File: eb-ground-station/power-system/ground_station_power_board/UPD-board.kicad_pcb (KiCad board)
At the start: 2 copper layers, 140.7 x 86.5 mm, 185 parts, among them J1 Conn_01x04, J10 PI 1827486, J11 PC 1720806, J12 Conn_02x02_Odd_Even, J13 Conn_01x05, J14 Conn_01x04, J2 Conn_01x03, J3 Conn_01x03, J4 Conn_01x03, J5 Conn_01x03, J6 Conn_01x03, J7 PI 1924143, J8 PI 1827923, J9 PI 1827486, Q1 DMN61D8L-LVT, Q10 DMN61D8L-LVT, Q11 SUD50P08-25L-E3, Q12 SUD50P08-25L-E3, Q13 DMN61D8L-LVT, Q14 DMN61D8L-LVT, Q15 DMN61D8L-LVT, Q16 DMN61D8L-LVT, Q17 DMN61D8L-LVT, Q18 DMN61D8L-LVT, Q19 DMN61D8L-LVT, Q2 SUD50P08-25L-E3, Q20 DMN61D8L-LVT, Q21 SUD50P08-25L-E3, Q22 SUD50P08-25L-E3, Q3 SUD50P08-25L-E3, Q4 DMN61D8L-LVT, Q5 SUD50P08-25L-E3, Q6 SUD50P08-25L-E3, Q7 DMN61D8L-LVT, Q8 SUD50P08-25L-E3, Q9 SUD50P08-25L-E3, U1 MAX7310, U10 TC4427, U11 TC4427, U12 TC4427, U13 TC4427, U14 TC4427, U15 TC4427, U2 MAX7310, U3 MAX7310, U4 ADT7410TRZ, U5 ADS1115IDGS, U6 UA78M33, U7 U_RasPi_40pin, U8 TC4427, U9 TC4427

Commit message: Cleaned up the repo
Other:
- board text removed: "Different analog connector"
- board text removed: "TODO:"
- board text removed: "Too many vias in high current traces?"
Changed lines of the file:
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@@
-    (effects (font (size 1.5 1.5) (thickness 0.3)))
-  )
-  (gr_text "Different analog connector" (at 29.4386 21.4122) (layer "F.Cu")
-    (effects (font (size 1.5 1.5) (thickness 0.3)))
-  )
-  (gr_text "TODO:" (at 20.955 16.5608) (layer "F.Cu")
-    (effects (font (size 3 3) (thickness 0.3)))
-  )
-  (gr_text "Too many vias in high current traces?" (at 35.9156 24.9174) (layer "F.Cu")
     (effects (font (size 1.5 1.5) (thickness 0.3)))
   )

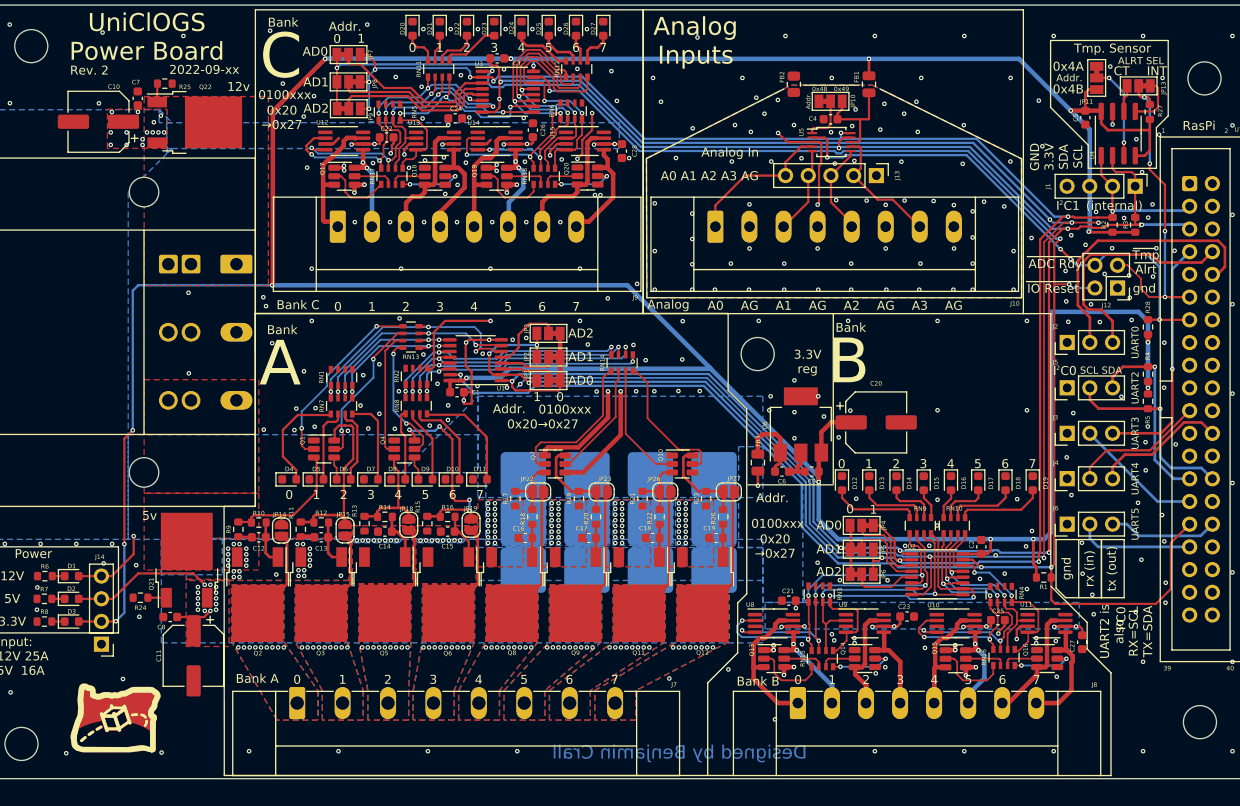
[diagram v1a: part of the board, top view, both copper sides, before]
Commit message: Fixed UPD board, ready for review and ordering
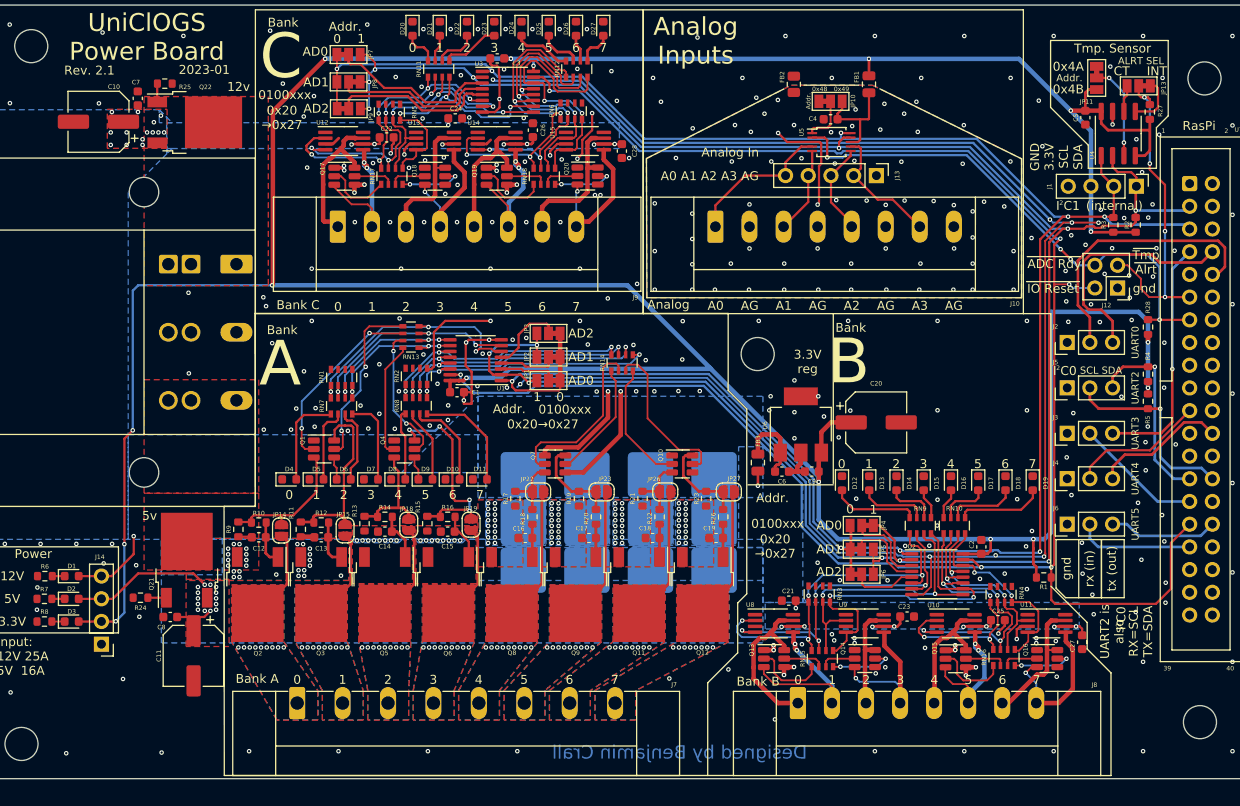
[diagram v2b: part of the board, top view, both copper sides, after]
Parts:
- removed LOGO1: OreSat Logo, oresat-footprints:logo-small
- moved R2 2.59 mm to (203.3, 77.8)
- moved R3 2.45 mm to (200.8, 77.8)
- moved J1 0.14 mm to (203.4, 73.5)
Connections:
- J1 pad 1: SCL -> SDA
- J1 pad 2: SDA -> SCL
- Q1 pad 2: MOS_A0 -> MOS_A1
- Q1 pad 5: MOS_A1 -> MOS_A0
- Q10 pad 2: MOS_A6 -> MOS_A7
- Q10 pad 5: MOS_A7 -> MOS_A6
- Q13 pad 3: OUT_B0 -> OUT_B1
- Q13 pad 6: OUT_B1 -> OUT_B0
- Q14 pad 3: OUT_B2 -> OUT_B3
- Q14 pad 6: OUT_B3 -> OUT_B2
- Q15 pad 3: OUT_B4 -> OUT_B5
- Q15 pad 6: OUT_B5 -> OUT_B4
- Q16 pad 3: OUT_B6 -> OUT_B7
- Q16 pad 6: OUT_B7 -> OUT_B6
- Q17 pad 3: OUT_C0 -> OUT_C1
- Q17 pad 6: OUT_C1 -> OUT_C0
- Q18 pad 3: OUT_C2 -> OUT_C3
- Q18 pad 6: OUT_C3 -> OUT_C2
- Q19 pad 3: OUT_C4 -> OUT_C5
- Q19 pad 6: OUT_C5 -> OUT_C4
- Q20 pad 3: OUT_C6 -> OUT_C7
- Q20 pad 6: OUT_C7 -> OUT_C6
- Q4 pad 2: MOS_A2 -> MOS_A3
- Q4 pad 5: MOS_A3 -> MOS_A2
- Q7 pad 2: MOS_A4 -> MOS_A5
- Q7 pad 5: MOS_A5 -> MOS_A4
- U4 pad 1: SDA -> SCL
- U4 pad 2: SCL -> SDA
- U5 pad 10: SDA -> SCL
- U5 pad 9: SCL -> SDA
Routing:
- net OUT_B1: track 12.4 -> 21.4 mm
- net OUT_B3: track 10.1 -> 17.2 mm, vias 0 -> 1
- net MOS_A5: track 13.1 -> 19.7 mm
- net OUT_C1: track 11.4 -> 16.5 mm
- net OUT_B5: track 11.4 -> 16.0 mm
- net MOS_A6: track 13.6 -> 18.2 mm
- net OUT_B7: track 12.4 -> 16.8 mm, vias 0 -> 1
- net OUT_C5: track 11.3 -> 15.6 mm
- net SCL: track 256.6 -> 252.3 mm
- net OUT_C3: track 10.9 -> 15.0 mm, vias 0 -> 1
- net MOS_A1: track 16.9 -> 21.0 mm
- net MOS_A4: track 17.2 -> 13.2 mm
- net OUT_C7: track 12.1 -> 15.8 mm, vias 0 -> 1
- net SDA: track 254.0 -> 256.7 mm, vias 14 -> 13
- net MOS_A7: track 16.0 -> 13.9 mm
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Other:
- board text added: "2023-01"
- board text added: "GND 3.3V SCL SDA"
- board text added: "Rev. 2.1"
- board text removed: "2022-09-xx"
- board text removed: "GND 3.3V SDA SCL"
- board text removed: "Rev. 2"

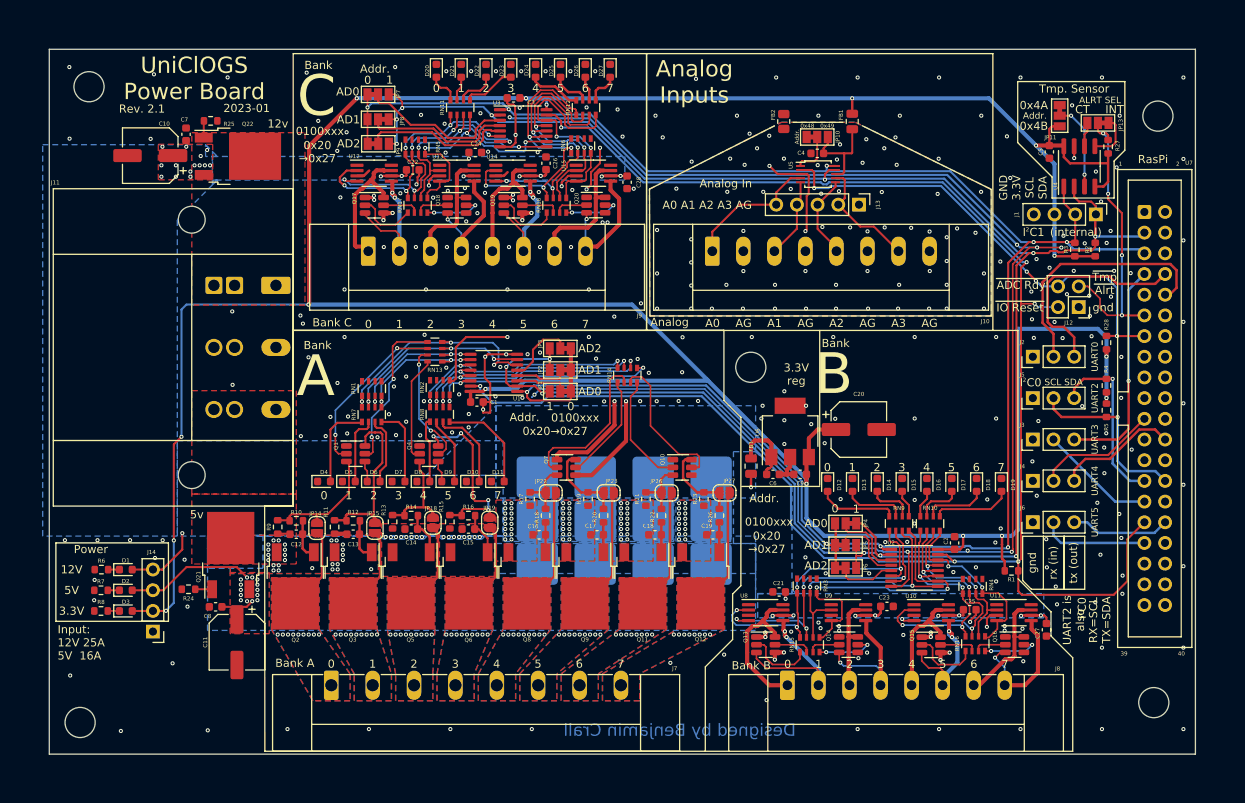
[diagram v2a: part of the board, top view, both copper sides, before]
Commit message: Fixed pin 1 of expanders being pulldown only
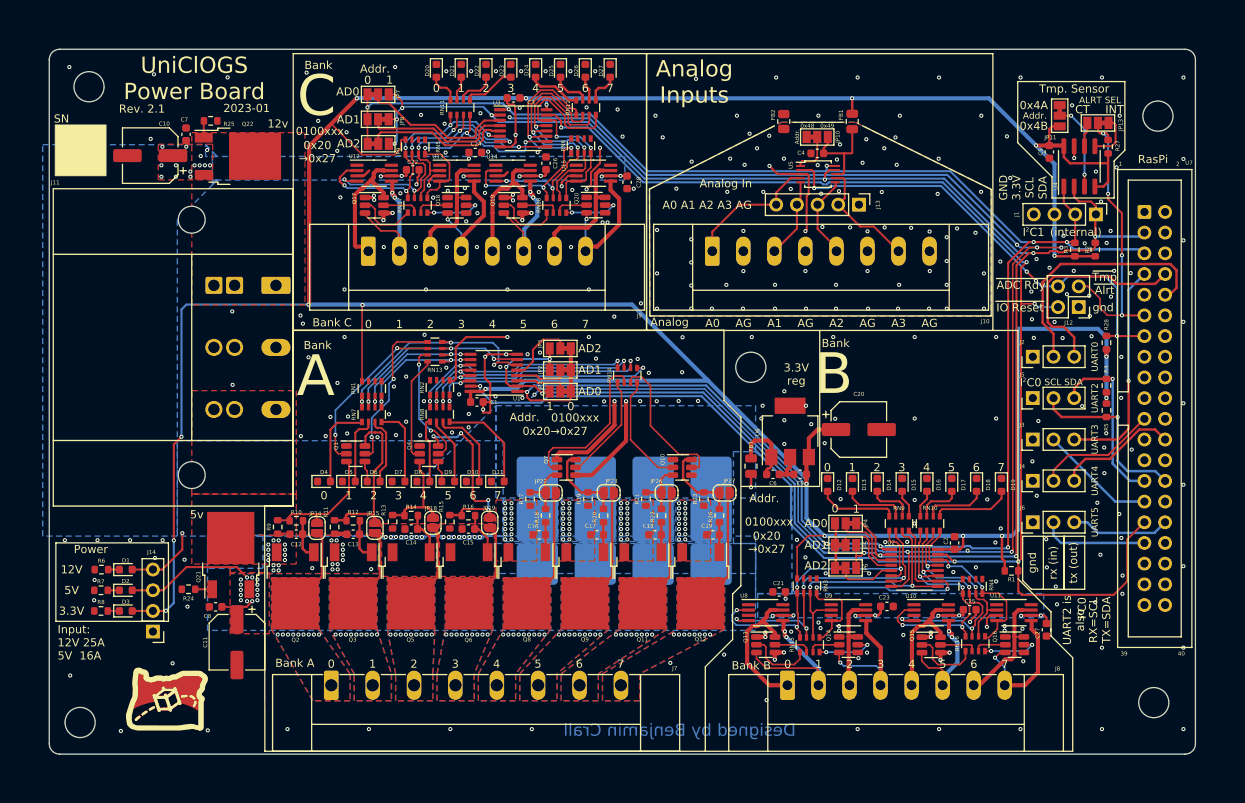
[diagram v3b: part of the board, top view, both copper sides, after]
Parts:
- added LOGO1: OreSat Logo, oresat-graphics:logo-small, F.Cu at (89.2, 132.7)
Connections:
- RN1 pad 4: GND -> +3V3
- RN3 pad 4: GND -> +3V3
- RN5 pad 4: GND -> +3V3
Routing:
- net +3V3: track 432.0 -> 461.1 mm, vias 16 -> 18
- net GND: vias 273 -> 274
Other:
- outline, holes or cut-outs redrawn
- board text added: "SN"
